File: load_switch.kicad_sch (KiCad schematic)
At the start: 5 parts, among them U6 FPF2701MPX

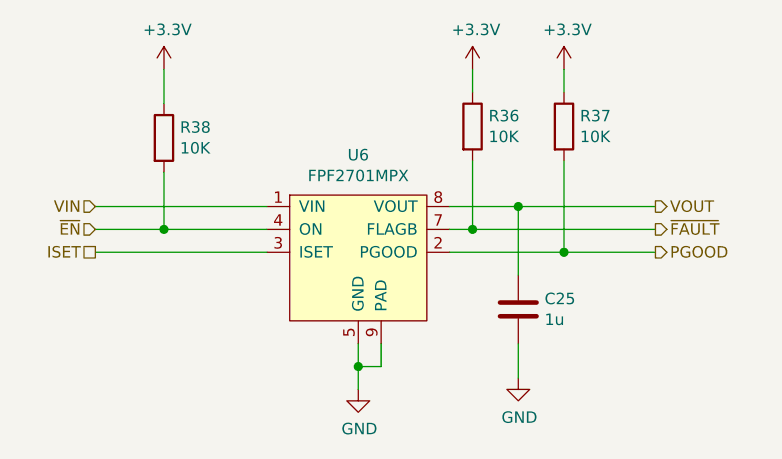
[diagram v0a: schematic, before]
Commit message: Started new connector layout
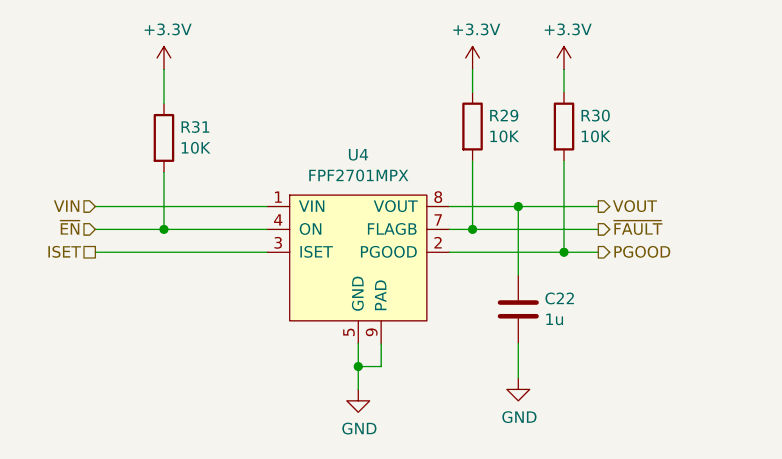
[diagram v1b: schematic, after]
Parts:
- renumbered C25 to C22, R36 to R29, R37 to R30, R38 to R31, U6 to U4
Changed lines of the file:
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@@
     (stroke (width 0) (type solid) (color 0 0 0 0))
   )
-  (wire (pts (xy 157.48 97.79) (xy 177.8 97.79))
+  (wire (pts (xy 157.48 97.79) (xy 171.45 97.79))
     (stroke (width 0) (type solid) (color 0 0 0 0))
   )
-  (wire (pts (xy 162.56 95.25) (xy 177.8 95.25))
+  (wire (pts (xy 162.56 95.25) (xy 171.45 95.25))
     (stroke (width 0) (type solid) (color 0 0 0 0))
   )
@@
     (stroke (width 0) (type solid) (color 0 0 0 0))
   )
-  (wire (pts (xy 167.64 100.33) (xy 177.8 100.33))
+  (wire (pts (xy 167.64 100.33) (xy 171.45 100.33))
     (stroke (width 0) (type solid) (color 0 0 0 0))
   )
@@
     (effects (font (size 1.27 1.27)) (justify right))
   )
-  (hierarchical_label "VOUT" (shape output) (at 177.8 95.25 0)
+  (hierarchical_label "VOUT" (shape output) (at 171.45 95.25 0)
     (effects (font (size 1.27 1.27)) (justify left))
   )
-  (hierarchical_label "~FAULT" (shape output) (at 177.8 97.79 0)
+  (hierarchical_label "~FAULT" (shape output) (at 171.45 97.79 0)
     (effects (font (size 1.27 1.27)) (justify left))
   )
-  (hierarchical_label "PGOOD" (shape output) (at 177.8 100.33 0)
+  (hierarchical_label "PGOOD" (shape output) (at 171.45 100.33 0)
     (effects (font (size 1.27 1.27)) (justify left))
   )
   (symbol (lib_id "power:+3.3V") (at 123.19 80.01 0)
     (in_bom yes) (on_board yes)
-    (property "Reference" "#PWR072" (id 0) (at 123.19 83.82 0)
+    (property "Reference" "#PWR050" (id 0) (at 123.19 83.82 0)
       (effects (font (size 1.27 1.27)) hide)
     )
@@
   (symbol (lib_id "power:+3.3V") (at 157.48 80.01 0)
     (in_bom yes) (on_board yes)
-    (property "Reference" "#PWR073" (id 0) (at 157.48 83.82 0)
+    (property "Reference" "#PWR051" (id 0) (at 157.48 83.82 0)
       (effects (font (size 1.27 1.27)) hide)
     )
@@
   (symbol (lib_id "power:+3.3V") (at 167.64 80.01 0)
     (in_bom yes) (on_board yes)
-    (property "Reference" "#PWR074" (id 0) (at 167.64 83.82 0)
+    (property "Reference" "#PWR052" (id 0) (at 167.64 83.82 0)
       (effects (font (size 1.27 1.27)) hide)
     )
@@
   (symbol (lib_id "power:GND") (at 144.78 115.57 0)
     (in_bom yes) (on_board yes)
-    (property "Reference" "#PWR076" (id 0) (at 144.78 121.92 0)
+    (property "Reference" "#PWR054" (id 0) (at 144.78 121.92 0)
       (effects (font (size 1.27 1.27)) hide)
     )
@@
   (symbol (lib_id "power:GND") (at 162.56 114.3 0)
     (in_bom yes) (on_board yes)
-    (property "Reference" "#PWR075" (id 0) (at 162.56 120.65 0)
+    (property "Reference" "#PWR053" (id 0) (at 162.56 120.65 0)
       (effects (font (size 1.27 1.27)) hide)
     )
@@
   (symbol (lib_id "Device:R") (at 123.19 87.63 0)
     (in_bom yes) (on_board yes)
-    (property "Reference" "R38" (id 0) (at 124.968 86.4616 0)
+    (property "Reference" "R31" (id 0) (at 124.968 86.4616 0)
       (effects (font (size 1.27 1.27)) (justify left))
     )
@@
   (symbol (lib_id "Device:R") (at 157.48 86.36 0)
     (in_bom yes) (on_board yes)
-    (property "Reference" "R36" (id 0) (at 159.258 85.1916 0)
+    (property "Reference" "R29" (id 0) (at 159.258 85.1916 0)
       (effects (font (size 1.27 1.27)) (justify left))
     )
@@
   (symbol (lib_id "Device:R") (at 167.64 86.36 0)
     (in_bom yes) (on_board yes)
-    (property "Reference" "R37" (id 0) (at 169.418 85.1916 0)
+    (property "Reference" "R30" (id 0) (at 169.418 85.1916 0)
       (effects (font (size 1.27 1.27)) (justify left))
     )
@@
   (symbol (lib_id "Device:C") (at 162.56 106.68 0)
     (in_bom yes) (on_board yes)
-    (property "Reference" "C25" (id 0) (at 165.481 105.5116 0)
+    (property "Reference" "C22" (id 0) (at 165.481 105.5116 0)
       (effects (font (size 1.27 1.27)) (justify left))
     )
@@
   (symbol (lib_id "IC_WUT:FPF270xMPX") (at 144.78 97.79 0)
     (in_bom yes) (on_board yes)
-    (property "Reference" "U6" (id 0) (at 144.78 89.535 0))
+    (property "Reference" "U4" (id 0) (at 144.78 89.535 0))
     (property "Value" "FPF2701MPX" (id 1) (at 144.78 91.8464 0))
     (property "Footprint" "IC_WUT:WDFN-8-1EP_3x3mm_P0.65mm_EP1.7x2.52mm" (id 2) (at 148.59 76.2 0)

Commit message: Mostly complete, just missing a few tracks and review
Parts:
- C22: footprint Capacitor_SMD:C_0402_1005Metric -> Capacitor_SMD:C_0603_1608Metric
- R34: renamed from R29; footprint Resistor_SMD:R_0402_1005Metric -> Resistor_SMD:R_0603_1608Metric
- R35: renamed from R30; footprint Resistor_SMD:R_0402_1005Metric -> Resistor_SMD:R_0603_1608Metric
- R36: renamed from R31; footprint Resistor_SMD:R_0402_1005Metric -> Resistor_SMD:R_0603_1608Metric
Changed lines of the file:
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@@
   (symbol (lib_id "power:+3.3V") (at 123.19 80.01 0)
     (in_bom yes) (on_board yes)
-    (property "Reference" "#PWR050" (id 0) (at 123.19 83.82 0)
+    (property "Reference" "#PWR051" (id 0) (at 123.19 83.82 0)
       (effects (font (size 1.27 1.27)) hide)
     )
@@
   (symbol (lib_id "power:+3.3V") (at 157.48 80.01 0)
     (in_bom yes) (on_board yes)
-    (property "Reference" "#PWR051" (id 0) (at 157.48 83.82 0)
+    (property "Reference" "#PWR052" (id 0) (at 157.48 83.82 0)
       (effects (font (size 1.27 1.27)) hide)
     )
@@
   (symbol (lib_id "power:+3.3V") (at 167.64 80.01 0)
     (in_bom yes) (on_board yes)
-    (property "Reference" "#PWR052" (id 0) (at 167.64 83.82 0)
+    (property "Reference" "#PWR053" (id 0) (at 167.64 83.82 0)
       (effects (font (size 1.27 1.27)) hide)
     )
@@
   (symbol (lib_id "power:GND") (at 144.78 115.57 0)
     (in_bom yes) (on_board yes)
-    (property "Reference" "#PWR054" (id 0) (at 144.78 121.92 0)
+    (property "Reference" "#PWR055" (id 0) (at 144.78 121.92 0)
       (effects (font (size 1.27 1.27)) hide)
     )
@@
   (symbol (lib_id "power:GND") (at 162.56 114.3 0)
     (in_bom yes) (on_board yes)
-    (property "Reference" "#PWR053" (id 0) (at 162.56 120.65 0)
+    (property "Reference" "#PWR054" (id 0) (at 162.56 120.65 0)
       (effects (font (size 1.27 1.27)) hide)
     )
@@
   (symbol (lib_id "Device:R") (at 123.19 87.63 0)
     (in_bom yes) (on_board yes)
-    (property "Reference" "R31" (id 0) (at 124.968 86.4616 0)
+    (property "Reference" "R36" (id 0) (at 124.968 86.4616 0)
       (effects (font (size 1.27 1.27)) (justify left))
     )
@@
       (effects (font (size 1.27 1.27)) (justify left))
     )
-    (property "Footprint" "Resistor_SMD:R_0402_1005Metric" (id 2) (at 121.412 87.63 90)
+    (property "Footprint" "Resistor_SMD:R_0603_1608Metric" (id 2) (at 121.412 87.63 90)
       (effects (font (size 1.27 1.27)) hide)
     )
@@
   (symbol (lib_id "Device:R") (at 157.48 86.36 0)
     (in_bom yes) (on_board yes)
-    (property "Reference" "R29" (id 0) (at 159.258 85.1916 0)
+    (property "Reference" "R34" (id 0) (at 159.258 85.1916 0)
       (effects (font (size 1.27 1.27)) (justify left))
     )
@@
       (effects (font (size 1.27 1.27)) (justify left))
     )
-    (property "Footprint" "Resistor_SMD:R_0402_1005Metric" (id 2) (at 155.702 86.36 90)
+    (property "Footprint" "Resistor_SMD:R_0603_1608Metric" (id 2) (at 155.702 86.36 90)
       (effects (font (size 1.27 1.27)) hide)
     )
@@
   (symbol (lib_id "Device:R") (at 167.64 86.36 0)
     (in_bom yes) (on_board yes)
-    (property "Reference" "R30" (id 0) (at 169.418 85.1916 0)
+    (property "Reference" "R35" (id 0) (at 169.418 85.1916 0)
       (effects (font (size 1.27 1.27)) (justify left))
     )
@@
       (effects (font (size 1.27 1.27)) (justify left))
     )
-    (property "Footprint" "Resistor_SMD:R_0402_1005Metric" (id 2) (at 165.862 86.36 90)
+    (property "Footprint" "Resistor_SMD:R_0603_1608Metric" (id 2) (at 165.862 86.36 90)
       (effects (font (size 1.27 1.27)) hide)
     )
@@
       (effects (font (size 1.27 1.27)) (justify left))
     )
-    (property "Footprint" "Capacitor_SMD:C_0402_1005Metric" (id 2) (at 163.5252 110.49 0)
+    (property "Footprint" "Capacitor_SMD:C_0603_1608Metric" (id 2) (at 163.5252 110.49 0)
       (effects (font (size 1.27 1.27)) hide)
     )

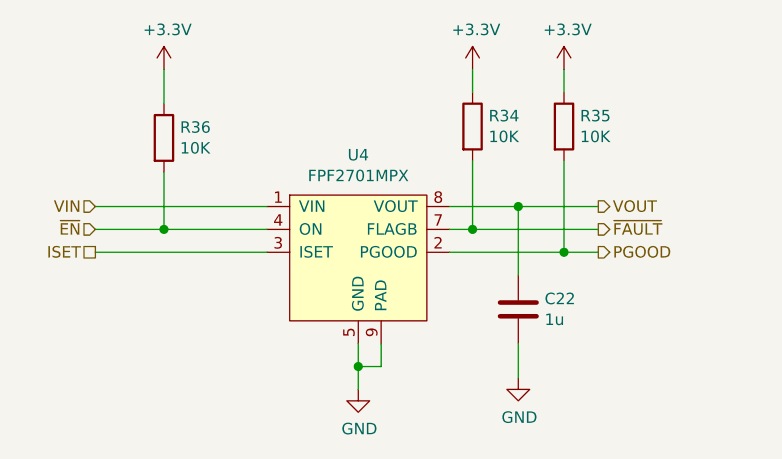
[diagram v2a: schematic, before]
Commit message: Finished tidying up silkscreen
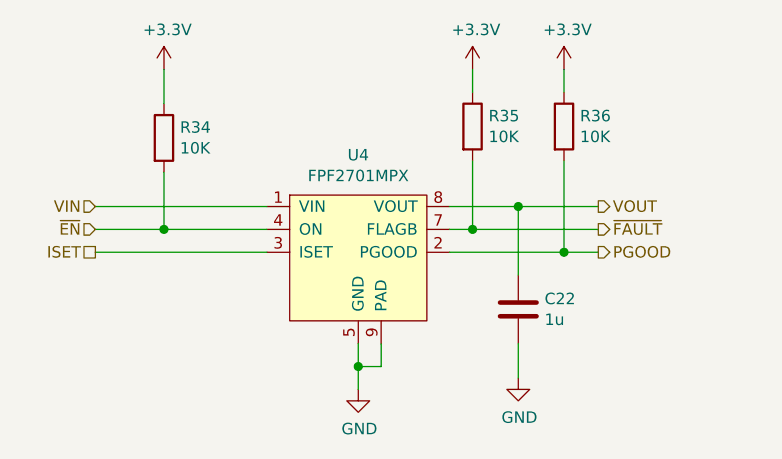
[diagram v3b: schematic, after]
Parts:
- renumbered R36 to R34, R34 to R35, R35 to R36
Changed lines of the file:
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@@
   (symbol (lib_id "power:+3.3V") (at 157.48 80.01 0)
     (in_bom yes) (on_board yes)
-    (property "Reference" "#PWR052" (id 0) (at 157.48 83.82 0)
+    (property "Reference" "#PWR053" (id 0) (at 157.48 83.82 0)
       (effects (font (size 1.27 1.27)) hide)
     )
@@
   (symbol (lib_id "power:+3.3V") (at 167.64 80.01 0)
     (in_bom yes) (on_board yes)
-    (property "Reference" "#PWR053" (id 0) (at 167.64 83.82 0)
+    (property "Reference" "#PWR055" (id 0) (at 167.64 83.82 0)
       (effects (font (size 1.27 1.27)) hide)
     )
@@
   (symbol (lib_id "power:GND") (at 144.78 115.57 0)
     (in_bom yes) (on_board yes)
-    (property "Reference" "#PWR055" (id 0) (at 144.78 121.92 0)
+    (property "Reference" "#PWR052" (id 0) (at 144.78 121.92 0)
       (effects (font (size 1.27 1.27)) hide)
     )
@@
   (symbol (lib_id "Device:R") (at 123.19 87.63 0)
     (in_bom yes) (on_board yes)
-    (property "Reference" "R36" (id 0) (at 124.968 86.4616 0)
+    (property "Reference" "R34" (id 0) (at 124.968 86.4616 0)
       (effects (font (size 1.27 1.27)) (justify left))
     )
@@
   (symbol (lib_id "Device:R") (at 157.48 86.36 0)
     (in_bom yes) (on_board yes)
-    (property "Reference" "R34" (id 0) (at 159.258 85.1916 0)
+    (property "Reference" "R35" (id 0) (at 159.258 85.1916 0)
       (effects (font (size 1.27 1.27)) (justify left))
     )
@@
   (symbol (lib_id "Device:R") (at 167.64 86.36 0)
     (in_bom yes) (on_board yes)
-    (property "Reference" "R35" (id 0) (at 169.418 85.1916 0)
+    (property "Reference" "R36" (id 0) (at 169.418 85.1916 0)
       (effects (font (size 1.27 1.27)) (justify left))
     )
